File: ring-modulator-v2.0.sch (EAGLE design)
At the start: 26 parts, among them IC1 TL072D, U1 MC1496DR2G

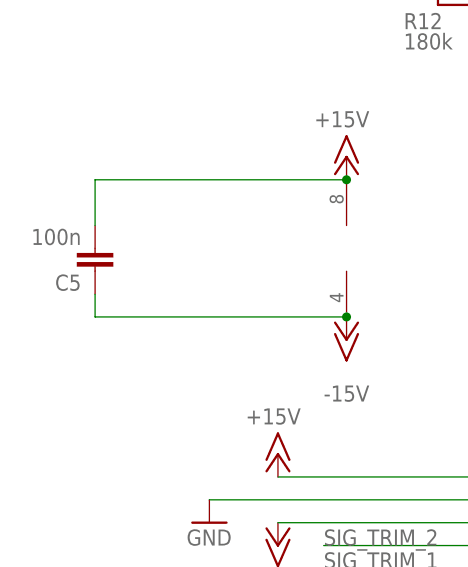
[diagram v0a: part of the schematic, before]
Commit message: Fixed silk screening, only missing xonik logo
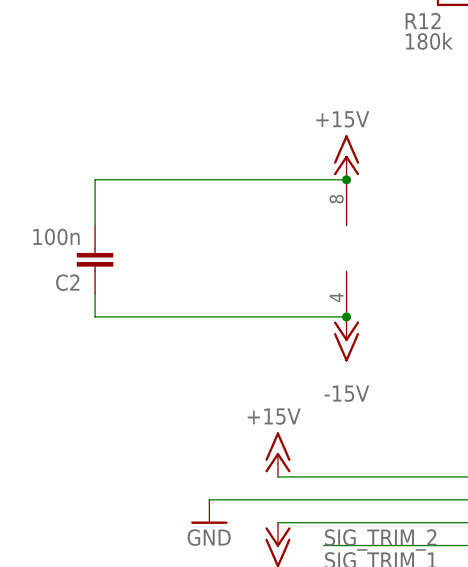
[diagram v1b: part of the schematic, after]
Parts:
- renumbered C5 to C2
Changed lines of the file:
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@@
 <part name="P+5" library="supply1" library_urn="urn:adsk.eagle:library:371" deviceset="+15V" device=""/>
 <part name="P-3" library="supply1" library_urn="urn:adsk.eagle:library:371" deviceset="-15V" device=""/>
-<part name="C5" library="resistor" deviceset="C-EU" device="C0805" value="100n"/>
+<part name="C2" library="resistor" deviceset="C-EU" device="C0805" value="100n"/>
 <part name="U$1" library="joakim" deviceset="MA10-1J" device="P"/>
 <part name="P+6" library="supply1" library_urn="urn:adsk.eagle:library:371" deviceset="+15V" device=""/>
@@
 <attribute name="VALUE" x="-15.24" y="22.86" size="1.778" layer="96" rot="R180"/>
 </instance>
-<instance part="C5" gate="G$1" x="-45.72" y="35.56" smashed="yes" rot="R180">
+<instance part="C2" gate="G$1" x="-45.72" y="35.56" smashed="yes" rot="R180">
 <attribute name="NAME" x="-47.244" y="35.179" size="1.778" layer="95" rot="R180"/>
 <attribute name="VALUE" x="-47.244" y="40.259" size="1.778" layer="96" rot="R180"/>
@@
 <pinref part="P-3" gate="1" pin="-15V"/>
 <junction x="-17.78" y="30.48"/>
-<pinref part="C5" gate="G$1" pin="1"/>
+<pinref part="C2" gate="G$1" pin="1"/>
 <wire x1="-45.72" y1="33.02" x2="-45.72" y2="30.48" width="0.1524" layer="91"/>
 <wire x1="-45.72" y1="30.48" x2="-17.78" y2="30.48" width="0.1524" layer="91"/>
@@
 <pinref part="IC1" gate="P" pin="V+"/>
 <pinref part="P+5" gate="1" pin="+15V"/>
-<pinref part="C5" gate="G$1" pin="2"/>
+<pinref part="C2" gate="G$1" pin="2"/>
 <wire x1="-45.72" y1="40.64" x2="-45.72" y2="45.72" width="0.1524" layer="91"/>
 <wire x1="-45.72" y1="45.72" x2="-17.78" y2="45.72" width="0.1524" layer="91"/>

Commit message: Added smd assembly bom etc
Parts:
- C1: value 100u 16V -> 100u 25V
- C2: device resistor:C-EUC0805 -> rcl:C-EUC0603
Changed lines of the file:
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@@
 <part name="R19" library="resistor" deviceset="R-EU_" device="R0805" value="1k5"/>
 <part name="P+2" library="supply1" library_urn="urn:adsk.eagle:library:371" deviceset="+15V" device=""/>
-<part name="C1" library="joakim-jclpcb" deviceset="VZL101M1CTR-0606" device="" value="100u 16V"/>
+<part name="C1" library="joakim-jclpcb" deviceset="VZL101M1CTR-0606" device="" value="100u 25V"/>
 <part name="GND3" library="supply1" library_urn="urn:adsk.eagle:library:371" deviceset="GND" device=""/>
 <part name="R13" library="resistor" deviceset="R-EU_" device="R0805" value="6k8"/>
@@
 <part name="P+5" library="supply1" library_urn="urn:adsk.eagle:library:371" deviceset="+15V" device=""/>
 <part name="P-3" library="supply1" library_urn="urn:adsk.eagle:library:371" deviceset="-15V" device=""/>
-<part name="C2" library="resistor" deviceset="C-EU" device="C0805" value="100n"/>
+<part name="C2" library="rcl" library_urn="urn:adsk.eagle:library:334" deviceset="C-EU" device="C0603" package3d_urn="urn:adsk.eagle:package:23616/2" value="100n"/>
 <part name="U$1" library="joakim" deviceset="MA10-1J" device="P"/>
 <part name="P+6" library="supply1" library_urn="urn:adsk.eagle:library:371" deviceset="+15V" device=""/>
@@
 <instance part="C1" gate="G$1" x="-17.78" y="99.06" smashed="yes" rot="R270">
 <attribute name="NAME" x="-17.2974" y="97.917" size="1.778" layer="95" rot="R270"/>
-<attribute name="VALUE" x="-24.257" y="102.0826" size="1.778" layer="96"/>
+<attribute name="VALUE" x="-23.3426" y="92.583" size="1.778" layer="96" rot="R90"/>
 </instance>
 <instance part="GND3" gate="1" x="-17.78" y="91.44" smashed="yes">
@@
 will not be understood (or retained) with this version.
 </note>
+<note version="8.3" severity="warning">
+Since Version 8.3, EAGLE supports the association of 3D packages
+with devices in libraries, schematics, and board files. Those 3D
+packages will not be understood (or retained) with this version.
+</note>
+<note version="8.4" severity="warning">
+Since Version 8.4, EAGLE supports properties for SPICE simulation.
+Probes in schematics and SPICE mapping objects found in parts and library devices
+will not be understood with this version. Update EAGLE to the latest version
+for full support of SPICE simulation.
+</note>
 </compatibility>

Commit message: Added info about external trimmers
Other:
- note added: "+15V"
- note added: "-15V"
- note added: "220R"
- note added: "500R"
- moved on the sheet: U$1
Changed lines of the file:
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@@
 <sheet>
 <plain>
+<wire x1="7.62" y1="109.22" x2="12.7" y2="109.22" width="0.1524" layer="97"/>
+<wire x1="10.16" y1="111.76" x2="12.7" y2="109.22" width="0.1524" layer="97"/>
+<wire x1="12.7" y1="109.22" x2="15.24" y2="111.76" width="0.1524" layer="97"/>
+<wire x1="15.24" y1="111.76" x2="12.7" y2="111.76" width="0.1524" layer="97"/>
+<wire x1="12.7" y1="111.76" x2="10.16" y2="111.76" width="0.1524" layer="97"/>
+<wire x1="12.7" y1="111.76" x2="12.7" y2="116.84" width="0.1524" layer="97"/>
+<wire x1="7.62" y1="104.14" x2="7.62" y2="109.22" width="0.1524" layer="97"/>
+<wire x1="12.7" y1="109.22" x2="17.78" y2="109.22" width="0.1524" layer="97"/>
+<wire x1="17.78" y1="109.22" x2="17.78" y2="104.14" width="0.1524" layer="97"/>
+<text x="17.78" y="111.76" size="1.778" layer="97">500R</text>
+<text x="10.16" y="119.38" size="1.778" layer="97">+15V</text>
+<wire x1="17.78" y1="27.94" x2="12.7" y2="27.94" width="0.1524" layer="97"/>
+<wire x1="15.24" y1="25.4" x2="12.7" y2="27.94" width="0.1524" layer="97"/>
+<wire x1="12.7" y1="27.94" x2="10.16" y2="25.4" width="0.1524" layer="97"/>
+<wire x1="10.16" y1="25.4" x2="12.7" y2="25.4" width="0.1524" layer="97"/>
+<wire x1="12.7" y1="25.4" x2="15.24" y2="25.4" width="0.1524" layer="97"/>
+<wire x1="12.7" y1="25.4" x2="12.7" y2="20.32" width="0.1524" layer="97"/>
+<wire x1="17.78" y1="33.02" x2="17.78" y2="27.94" width="0.1524" layer="97"/>
+<wire x1="12.7" y1="27.94" x2="7.62" y2="27.94" width="0.1524" layer="97"/>
+<wire x1="7.62" y1="27.94" x2="7.62" y2="33.02" width="0.1524" layer="97"/>
+<text x="17.78" y="22.86" size="1.778" layer="97">220R</text>
+<text x="15.24" y="17.78" size="1.778" layer="97" rot="R180">-15V</text>
 </plain>
 <instances>
@@
 <attribute name="VALUE" x="-47.244" y="40.259" size="1.778" layer="96" rot="R180"/>
 </instance>
-<instance part="U$1" gate="G$1" x="10.16" y="2.54" smashed="yes" rot="R180">
-<attribute name="VALUE" x="13.97" y="17.78" size="1.778" layer="96" rot="R180"/>
-<attribute name="NAME" x="13.97" y="-13.462" size="1.778" layer="95" rot="R180"/>
-</instance>
-<instance part="P+6" gate="1" x="-25.4" y="15.24" smashed="yes">
-<attribute name="VALUE" x="-22.86" y="20.32" size="1.778" layer="96" rot="R180"/>
-</instance>
-<instance part="P-4" gate="1" x="-25.4" y="5.08" smashed="yes">
-<attribute name="VALUE" x="-22.86" y="0" size="1.778" layer="96" rot="R180"/>
-</instance>
-<instance part="GND8" gate="1" x="-33.02" y="7.62" smashed="yes">
-<attribute name="VALUE" x="-35.56" y="5.08" size="1.778" layer="96"/>
+<instance part="U$1" gate="G$1" x="10.16" y="-2.54" smashed="yes" rot="R180">
+<attribute name="VALUE" x="13.97" y="12.7" size="1.778" layer="96" rot="R180"/>
+<attribute name="NAME" x="13.97" y="-18.542" size="1.778" layer="95" rot="R180"/>
+</instance>
+<instance part="P+6" gate="1" x="-25.4" y="10.16" smashed="yes">
+<attribute name="VALUE" x="-22.86" y="15.24" size="1.778" layer="96" rot="R180"/>
+</instance>
+<instance part="P-4" gate="1" x="-25.4" y="0" smashed="yes">
+<attribute name="VALUE" x="-22.86" y="-5.08" size="1.778" layer="96" rot="R180"/>
+</instance>
+<instance part="GND8" gate="1" x="-33.02" y="2.54" smashed="yes">
+<attribute name="VALUE" x="-35.56" y="0" size="1.778" layer="96"/>
 </instance>
 </instances>
@@
 <segment>
 <pinref part="U$1" gate="G$1" pin="4"/>
-<wire x1="-20.32" y1="5.08" x2="5.08" y2="5.08" width="0.1524" layer="91"/>
-<label x="-20.32" y="5.08" size="1.778" layer="95"/>
+<wire x1="-20.32" y1="0" x2="5.08" y2="0" width="0.1524" layer="91"/>
+<label x="-20.32" y="0" size="1.778" layer="95"/>
 </segment>
 </net>
@@
 <segment>
 <pinref part="U$1" gate="G$1" pin="5"/>
-<wire x1="5.08" y1="2.54" x2="-20.32" y2="2.54" width="0.1524" layer="91"/>
-<label x="-20.32" y="2.54" size="1.778" layer="95"/>
+<wire x1="5.08" y1="-2.54" x2="-20.32" y2="-2.54" width="0.1524" layer="91"/>
+<label x="-20.32" y="-2.54" size="1.778" layer="95"/>
 </segment>
 </net>
@@
 <segment>
 <pinref part="U$1" gate="G$1" pin="8"/>
-<wire x1="-20.32" y1="-5.08" x2="5.08" y2="-5.08" width="0.1524" layer="91"/>
-<label x="-20.32" y="-5.08" size="1.778" layer="95"/>
+<wire x1="-20.32" y1="-10.16" x2="5.08" y2="-10.16" width="0.1524" layer="91"/>
+<label x="-20.32" y="-10.16" size="1.778" layer="95"/>
 </segment>
 </net>
@@
 <segment>
 <pinref part="U$1" gate="G$1" pin="9"/>
-<wire x1="5.08" y1="-7.62" x2="-20.32" y2="-7.62" width="0.1524" layer="91"/>
-<label x="-20.32" y="-7.62" size="1.778" layer="95"/>
+<wire x1="5.08" y1="-12.7" x2="-20.32" y2="-12.7" width="0.1524" layer="91"/>
+<label x="-20.32" y="-12.7" size="1.778" layer="95"/>
 </segment>
 </net>
@@
 <pinref part="GND8" gate="1" pin="GND"/>
 <pinref part="U$1" gate="G$1" pin="2"/>
-<wire x1="-33.02" y1="10.16" x2="5.08" y2="10.16" width="0.1524" layer="91"/>
+<wire x1="-33.02" y1="5.08" x2="5.08" y2="5.08" width="0.1524" layer="91"/>
 </segment>
 </net>
@@
 <pinref part="U$1" gate="G$1" pin="3"/>
 <pinref part="P-4" gate="1" pin="-15V"/>
-<wire x1="5.08" y1="7.62" x2="-25.4" y2="7.62" width="0.1524" layer="91"/>
+<wire x1="5.08" y1="2.54" x2="-25.4" y2="2.54" width="0.1524" layer="91"/>
 </segment>
 </net>
@@
 <pinref part="P+6" gate="1" pin="+15V"/>
 <pinref part="U$1" gate="G$1" pin="1"/>
-<wire x1="-25.4" y1="12.7" x2="5.08" y2="12.7" width="0.1524" layer="91"/>
+<wire x1="-25.4" y1="7.62" x2="5.08" y2="7.62" width="0.1524" layer="91"/>
 </segment>
 </net>
@@
 <segment>
 <pinref part="U$1" gate="G$1" pin="10"/>
-<wire x1="-20.32" y1="-10.16" x2="5.08" y2="-10.16" width="0.1524" layer="91"/>
-<label x="-20.32" y="-10.16" size="1.778" layer="95"/>
+<wire x1="-20.32" y1="-15.24" x2="5.08" y2="-15.24" width="0.1524" layer="91"/>
+<label x="-20.32" y="-15.24" size="1.778" layer="95"/>
 </segment>
 </net>
@@
 <segment>
 <pinref part="U$1" gate="G$1" pin="7"/>
-<wire x1="5.08" y1="-2.54" x2="-20.32" y2="-2.54" width="0.1524" layer="91"/>
-<label x="-20.32" y="-2.54" size="1.778" layer="95"/>
+<wire x1="5.08" y1="-7.62" x2="-20.32" y2="-7.62" width="0.1524" layer="91"/>
+<label x="-20.32" y="-7.62" size="1.778" layer="95"/>
 </segment>
 </net>
@@
 <segment>
 <pinref part="U$1" gate="G$1" pin="6"/>
-<wire x1="-20.32" y1="0" x2="5.08" y2="0" width="0.1524" layer="91"/>
-<label x="-20.32" y="0" size="1.778" layer="95"/>
-</segment>
-</net>
+<wire x1="-20.32" y1="-5.08" x2="5.08" y2="-5.08" width="0.1524" layer="91"/>
+<label x="-20.32" y="-5.08" size="1.778" layer="95"/>
+</segment>
+</net>

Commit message: Added documentation from yusynth.net
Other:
- note added: "200 / 220R"
- note added: "470 / 500R"
- note removed: "220R"
- note removed: "500R"
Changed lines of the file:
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@@
 <layer number="88" name="SimResults" color="9" fill="1" visible="yes" active="yes"/>
 <layer number="89" name="SimProbes" color="9" fill="1" visible="yes" active="yes"/>
+<layer number="90" name="Modules" color="5" fill="1" visible="yes" active="yes"/>
 <layer number="91" name="Nets" color="2" fill="1" visible="yes" active="yes"/>
 <layer number="92" name="Busses" color="1" fill="1" visible="yes" active="yes"/>
@@
 <layer number="101" name="Patch_Top" color="7" fill="1" visible="no" active="no"/>
 <layer number="102" name="Vscore" color="7" fill="1" visible="yes" active="yes"/>
+<layer number="103" name="Accent_neu" color="7" fill="1" visible="yes" active="yes"/>
 <layer number="104" name="Name" color="7" fill="1" visible="yes" active="yes"/>
+<layer number="105" name="NXP" color="7" fill="1" visible="yes" active="yes"/>
+<layer number="106" name="NXP_2" color="7" fill="1" visible="yes" active="yes"/>
+<layer number="107" name="BD-Top" color="7" fill="1" visible="yes" active="yes"/>
+<layer number="108" name="fp8" color="7" fill="1" visible="yes" active="yes"/>
+<layer number="109" name="fp9" color="7" fill="1" visible="yes" active="yes"/>
+<layer number="110" name="fp0" color="7" fill="1" visible="yes" active="yes"/>
+<layer number="111" name="KASTMAAT1" color="7" fill="1" visible="yes" active="yes"/>
+<layer number="112" name="KASTMAAT2" color="7" fill="1" visible="yes" active="yes"/>
 <layer number="113" name="SERVICE" color="7" fill="1" visible="no" active="no"/>
+<layer number="114" name="FRNTMAAT1" color="7" fill="1" visible="yes" active="yes"/>
+<layer number="115" name="FRNTMAAT2" color="7" fill="1" visible="yes" active="yes"/>
 <layer number="116" name="Patch_BOT" color="7" fill="1" visible="no" active="no"/>
+<layer number="117" name="BACKMAAT1" color="7" fill="1" visible="yes" active="yes"/>
+<layer number="118" name="BACKMAAT2" color="7" fill="1" visible="yes" active="yes"/>
+<layer number="119" name="KAP_TEKEN" color="7" fill="1" visible="yes" active="yes"/>
+<layer number="120" name="KAP_MAAT1" color="7" fill="1" visible="yes" active="yes"/>
 <layer number="121" name="_tsilk" color="7" fill="1" visible="yes" active="yes"/>
 <layer number="122" name="_bsilk" color="7" fill="1" visible="yes" active="yes"/>
+<layer number="123" name="tTestmark" color="7" fill="1" visible="yes" active="yes"/>
+<layer number="124" name="bTestmark" color="7" fill="1" visible="yes" active="yes"/>
+<layer number="125" name="BIFRNTTEK" color="7" fill="1" visible="yes" active="yes"/>
+<layer number="126" name="BIFRNTMAT" color="7" fill="1" visible="yes" active="yes"/>
+<layer number="127" name="Info2" color="7" fill="1" visible="yes" active="yes"/>
+<layer number="130" name="SMDSTROOK" color="7" fill="1" visible="yes" active="yes"/>
+<layer number="131" name="tAdjust" color="7" fill="1" visible="yes" active="yes"/>
+<layer number="132" name="bAdjust" color="7" fill="1" visible="yes" active="yes"/>
+<layer number="133" name="BGA_CORE_SUP" color="12" fill="1" visible="yes" active="yes"/>
+<layer number="134" name="BGA_GND" color="1" fill="1" visible="yes" active="yes"/>
+<layer number="135" name="BGA_NC" color="8" fill="1" visible="yes" active="yes"/>
+<layer number="136" name="BGA_DED" color="14" fill="1" visible="yes" active="yes"/>
+<layer number="144" name="Drill_legend" color="7" fill="1" visible="yes" active="yes"/>
 <layer number="151" name="HeatSink" color="7" fill="1" visible="yes" active="yes"/>
+<layer number="199" name="Contour" color="7" fill="1" visible="yes" active="yes"/>
 <layer number="200" name="200bmp" color="1" fill="10" visible="no" active="no"/>
 <layer number="201" name="201bmp" color="2" fill="1" visible="no" active="no"/>
 <layer number="202" name="202bmp" color="3" fill="1" visible="no" active="no"/>
+<layer number="203" name="203bmp" color="7" fill="1" visible="yes" active="yes"/>
+<layer number="204" name="204bmp" color="7" fill="1" visible="yes" active="yes"/>
+<layer number="205" name="205bmp" color="7" fill="1" visible="yes" active="yes"/>
+<layer number="206" name="206bmp" color="7" fill="1" visible="yes" active="yes"/>
+<layer number="207" name="207bmp" color="7" fill="1" visible="yes" active="yes"/>
+<layer number="208" name="208bmp" color="7" fill="1" visible="yes" active="yes"/>
+<layer number="209" name="209bmp" color="7" fill="1" visible="yes" active="yes"/>
+<layer number="210" name="210bmp" color="7" fill="1" visible="yes" active="yes"/>
+<layer number="211" name="211bmp" color="7" fill="1" visible="yes" active="yes"/>
+<layer number="212" name="212bmp" color="7" fill="1" visible="yes" active="yes"/>
+<layer number="213" name="213bmp" color="7" fill="1" visible="yes" active="yes"/>
+<layer number="214" name="214bmp" color="7" fill="1" visible="yes" active="yes"/>
+<layer number="215" name="215bmp" color="7" fill="1" visible="yes" active="yes"/>
+<layer number="216" name="BottomExtra" color="7" fill="1" visible="yes" active="yes"/>
 <layer number="250" name="Descript" color="7" fill="1" visible="no" active="no"/>
 <layer number="251" name="SMDround" color="7" fill="1" visible="no" active="no"/>
 <layer number="254" name="cooling" color="7" fill="1" visible="yes" active="yes"/>
+<layer number="255" name="Accent" color="7" fill="1" visible="yes" active="yes"/>
 </layers>
 <schematic xreflabel="%F%N/%S.%C%R" xrefpart="/%S.%C%R">
@@
 <wire x1="12.7" y1="109.22" x2="17.78" y2="109.22" width="0.1524" layer="97"/>
 <wire x1="17.78" y1="109.22" x2="17.78" y2="104.14" width="0.1524" layer="97"/>
-<text x="17.78" y="111.76" size="1.778" layer="97">500R</text>
+<text x="17.78" y="111.76" size="1.778" layer="97">470 / 500R</text>
 <text x="10.16" y="119.38" size="1.778" layer="97">+15V</text>
 <wire x1="17.78" y1="27.94" x2="12.7" y2="27.94" width="0.1524" layer="97"/>
@@
 <wire x1="12.7" y1="27.94" x2="7.62" y2="27.94" width="0.1524" layer="97"/>
 <wire x1="7.62" y1="27.94" x2="7.62" y2="33.02" width="0.1524" layer="97"/>
-<text x="17.78" y="22.86" size="1.778" layer="97">220R</text>
+<text x="17.78" y="22.86" size="1.778" layer="97">200 / 220R</text>
 <text x="15.24" y="17.78" size="1.778" layer="97" rot="R180">-15V</text>
 </plain>

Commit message: moving
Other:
- note added: "DC inputs, add 1uF series caps for AC"
- note added: "DC output, add a 1uF series cap for AC"
- note added: "Trimming: Connect input caps (AC) Connect 1kHz sine to Carrier. Trim 200R (signal trim) until output is removed Connect 1kHz sine to Signal. Trim 500R (carrier trim) until output is removed"
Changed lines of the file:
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@@
 <text x="17.78" y="22.86" size="1.778" layer="97">200 / 220R</text>
 <text x="15.24" y="17.78" size="1.778" layer="97" rot="R180">-15V</text>
+<text x="-53.34" y="66.04" size="1.778" layer="97">DC inputs, add 1uF
+series caps for AC</text>
+<text x="154.94" y="63.5" size="1.778" layer="97">DC output, add a 1uF
+series cap for AC</text>
+<text x="-78.74" y="81.28" size="1.778" layer="97">Trimming:
+Connect input caps (AC)
+Connect 1kHz sine to Carrier.
+Trim 200R (signal trim) until output is removed
+Connect 1kHz sine to Signal.
+Trim 500R (carrier trim) until output is removed
+</text>
 </plain>
 <instances>
@@
 </drawing>
 <compatibility>
+<note version="6.3" minversion="6.2.2" severity="warning">
+Since Version 6.2.2 text objects can contain more than one line,
+which will not be processed correctly with this version.
+</note>
 <note version="8.2" severity="warning">
 Since Version 8.2, EAGLE supports online libraries. The ids
